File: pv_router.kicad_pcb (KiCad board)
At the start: 4 copper layers, 75 x 95 mm, 50 parts, among them IC1 L6981C33DR, IC2 ATM90E26-YU-B, IC3 ESP32-C3-WROOM-02-N4, J1 Barrel_Jack_Switch_Pin3Ring, J2 AudioJack3, J3 AudioJack3, J4 Barrel_Jack_Switch_Pin3Ring, J5 UART, J6 ToSSR, Q1 BSS138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

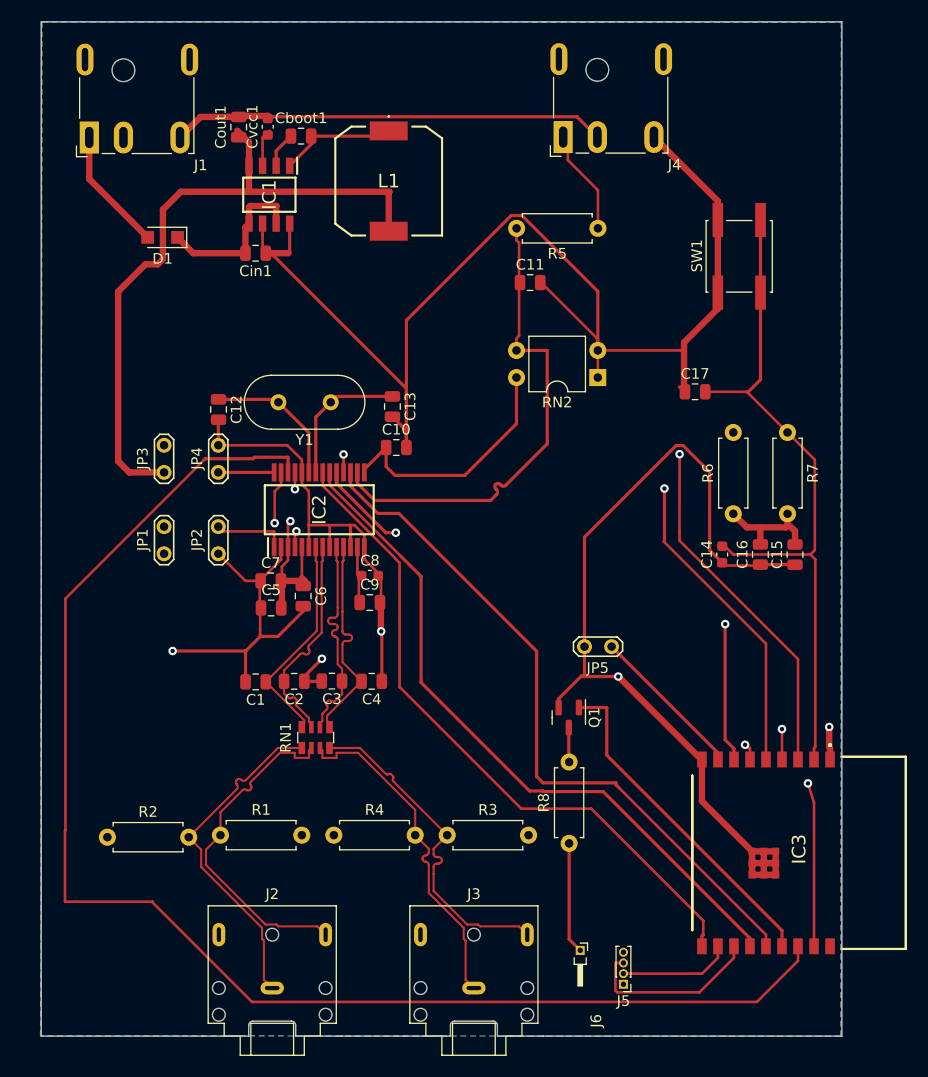
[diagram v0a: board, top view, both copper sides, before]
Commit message: PCB: root 4 layers, resize board
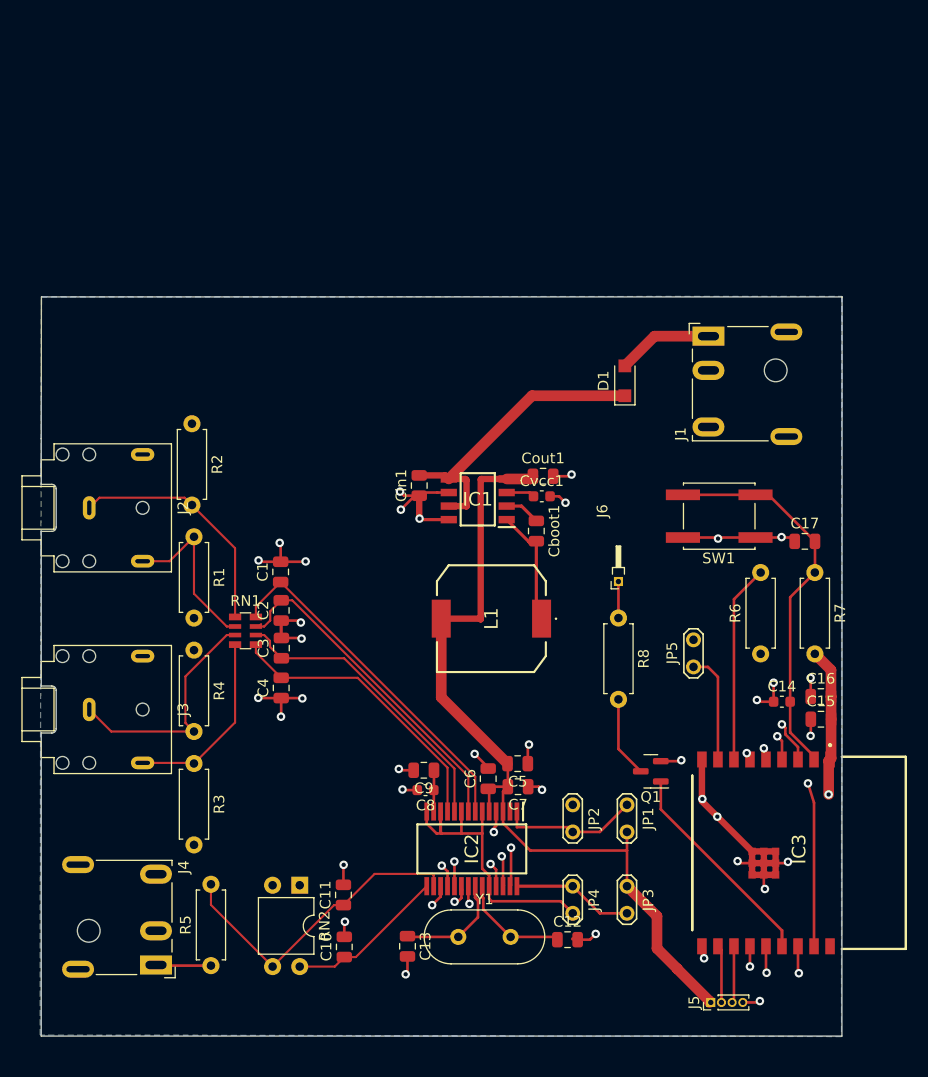
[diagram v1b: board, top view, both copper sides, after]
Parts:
- moved J4 86.4 mm to (135.8, 143.3), turned to -90 degrees
- moved R5 78.0 mm to (140.9, 143.4), turned to 90 degrees
- moved J1 60.9 mm to (187.5, 84.4), turned to 90 degrees
- moved C11 60.0 mm to (153.3, 136.8), turned to 90 degrees
- moved C12 59.5 mm to (174.3, 141.0), turned to 0 degrees
- moved JP3 58.2 mm to (179.9, 136.0), turned to -90 degrees
- moved RN2 55.1 mm to (149.2, 135.9), turned to -90 degrees
- moved Y1 51.5 mm to (164.1, 140.7), turned to 0 degrees
- moved JP4 51.0 mm to (174.8, 136.0), turned to -90 degrees
- moved C13 50.6 mm to (159.3, 141.6)
- moved JP1 49.3 mm to (179.9, 128.3), turned to -90 degrees
- moved J2 48.1 mm to (129.5, 100.5), turned to -90 degrees
- moved C10 47.0 mm to (153.4, 141.7), turned to 90 degrees
- moved D1 45.3 mm to (179.7, 88.6), turned to 90 degrees
- moved J3 44.5 mm to (129.5, 119.4), turned to -90 degrees
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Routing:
- net GND: track 532.2 -> 126.8 mm, vias 4 -> 35
- net /adc/SDO: track 131.7 -> 37.9 mm, vias 0 -> 2
- net +3V3: track 202.2 -> 118.5 mm, vias 2 -> 1
- net /adc/ZX: track 63.2 -> 27.0 mm, vias 0 -> 2
- net /adc/SCLK: track 65.6 -> 34.4 mm
- net /adc/IRQ: track 64.7 -> 34.3 mm, vias 0 -> 2
- net /esp32/EN: track 66.6 -> 36.5 mm
- net /adc/SDI: track 60.5 -> 30.8 mm
- net /adc/CF1: track 66.4 -> 43.6 mm
- net /adc/RESET: track 74.7 -> 52.6 mm
- net /adc/WarnOut: track 65.7 -> 47.0 mm, vias 0 -> 2
- net IC2-VP: track 45.8 -> 29.9 mm
- net I2N: track 32.0 -> 16.2 mm
- net /adc/CF2: track 55.1 -> 40.3 mm
- net Net-(IC3-IO8): track 33.3 -> 18.5 mm, vias 1 -> 0
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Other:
- board size 75 x 95 mm -> 75 x 69.2 mm

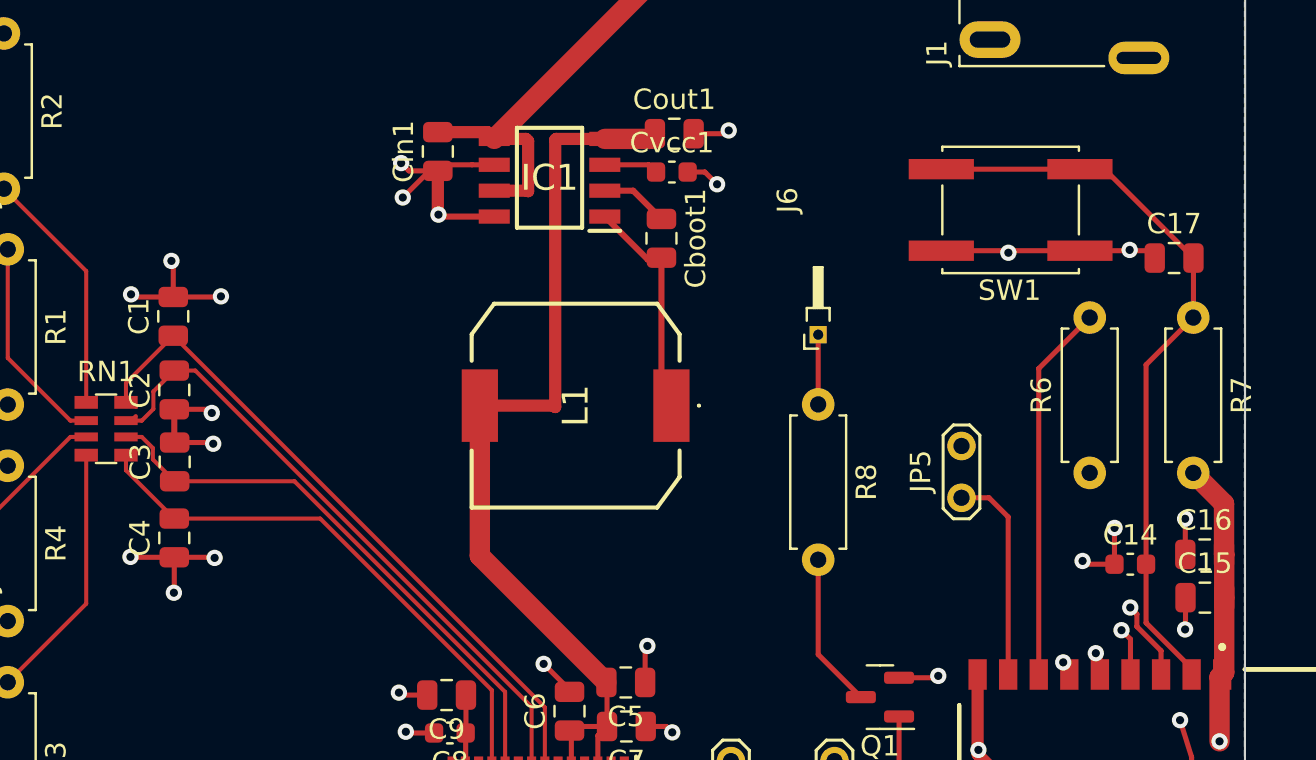
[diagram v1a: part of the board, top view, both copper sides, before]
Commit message: PCB: fix DRC errors
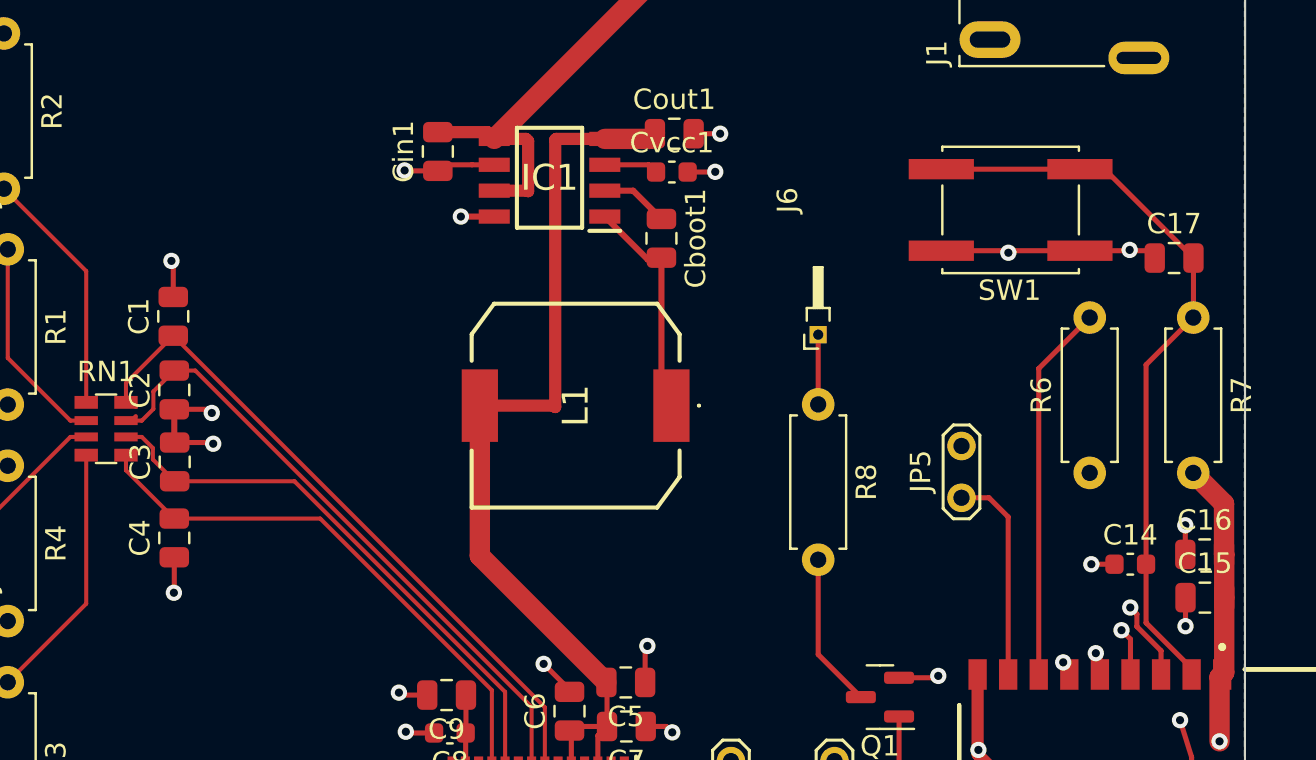
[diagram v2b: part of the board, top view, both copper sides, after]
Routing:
- net GND: track 126.8 -> 108.6 mm, vias 35 -> 29
- net /adc/IRQ: track 34.3 -> 39.8 mm

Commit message: PCB: fix some GND vias
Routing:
- net GND: track 108.6 -> 100.3 mm, vias 29 -> 33

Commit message: PCB: fix +3.3V track including zone
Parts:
- moved Cout1 12.2 mm to (161.7, 91.1), turned to 90 degrees
- moved Cin1 11.6 mm to (151.7, 90.8), turned to -90 degrees
- moved Cvcc1 11.1 mm to (162.4, 93.7)
- moved Cboot1 10.9 mm to (162.1, 97.0)
- moved IC1 10.9 mm to (156.6, 94.0)
- moved L1 7.31 mm to (162.6, 105.2), turned to 90 degrees
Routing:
- net Net-(D1-K): track 28.5 -> 35.7 mm
- net +3V3: track 118.5 -> 112.2 mm
- net GND: track 100.3 -> 97.6 mm, vias 33 -> 34
- net Net-(IC1-SW): track 12.3 -> 13.3 mm
- net /esp32/EN: vias 0 -> 1
- net Net-(IC3-IO8): vias 0 -> 1
- added copper zone on F.Cu, net +3V3

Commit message: PCB: fix GND tracks of ADC.
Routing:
- net GND: track 97.6 -> 77.8 mm, vias 34 -> 39
- net /adc/SDI: track 30.8 -> 30.1 mm

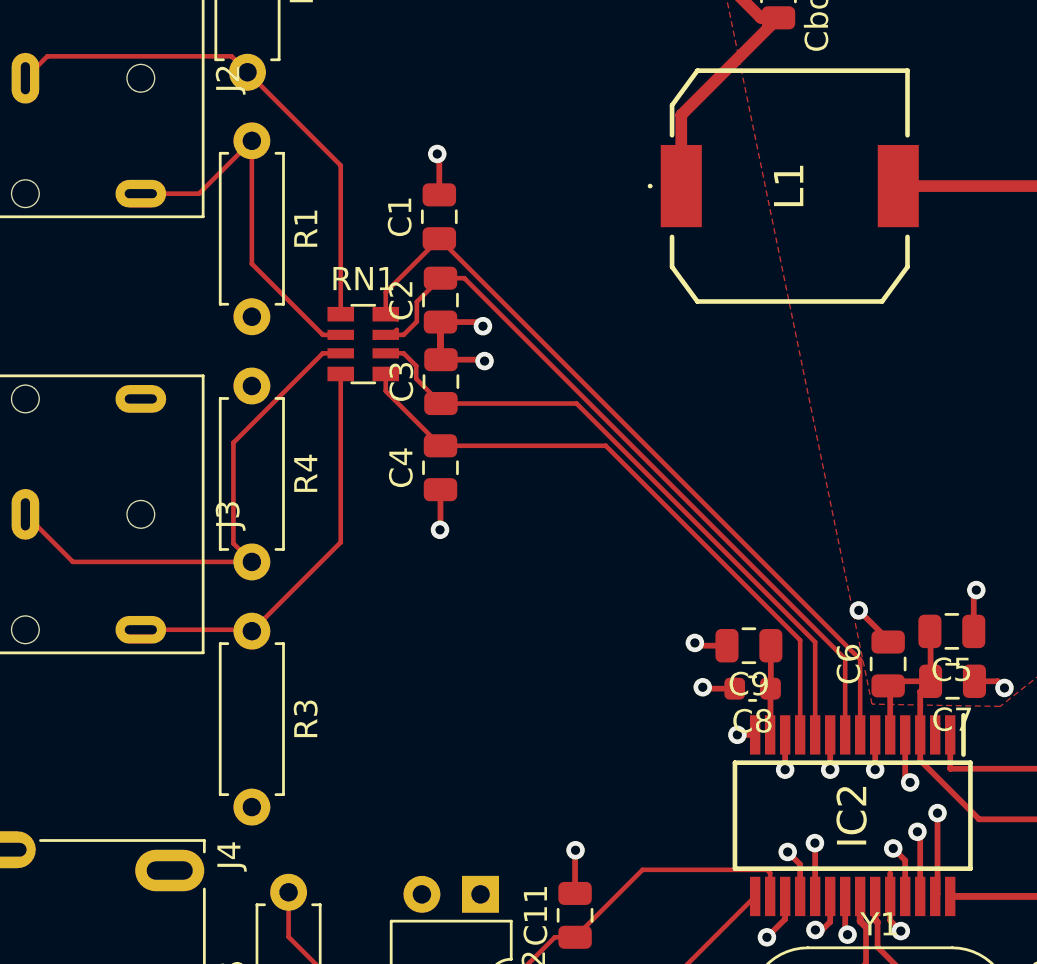
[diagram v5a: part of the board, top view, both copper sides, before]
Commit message: PCB: adjust length tracks of pairs I1 and I2
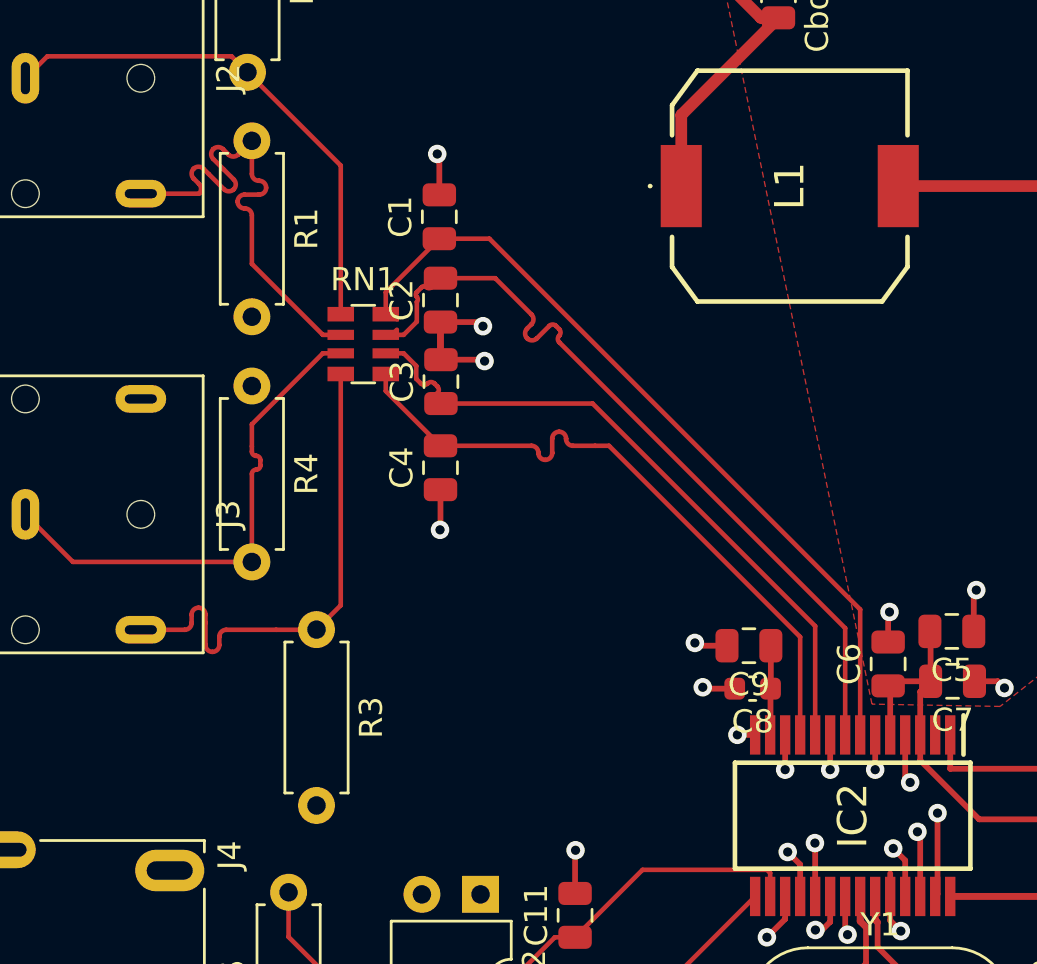
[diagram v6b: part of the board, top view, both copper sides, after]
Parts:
- moved R3 2.80 mm to (142.1, 124.4)
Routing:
- net I2N: track 16.2 -> 22.3 mm
- net I1N: track 17.6 -> 22.1 mm
- net IC2-I2N: track 32.1 -> 35.0 mm
- net IC2-I1N: track 27.6 -> 29.3 mm
- net IC2-I2P: track 33.9 -> 35.1 mm
- net IC2-I1P: track 28.1 -> 29.0 mm
- net GND: track 77.8 -> 77.3 mm
